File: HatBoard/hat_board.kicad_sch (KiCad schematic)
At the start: 18 parts, among them J10 Conn_02x02_Counter_Clockwise, J13 DF11 FC Connection, J14 Conn_02x02_Counter_Clockwise, J15 Conn_02x02_Counter_Clockwise, J19 DF11 FC Connection, J20 DF11 FC Connection, J21 DF11 FC Connection, J9 Conn_02x02_Counter_Clockwise, U10 VEML7700, U12 DRV2605LDGS, U27 TMP112AIDRLR

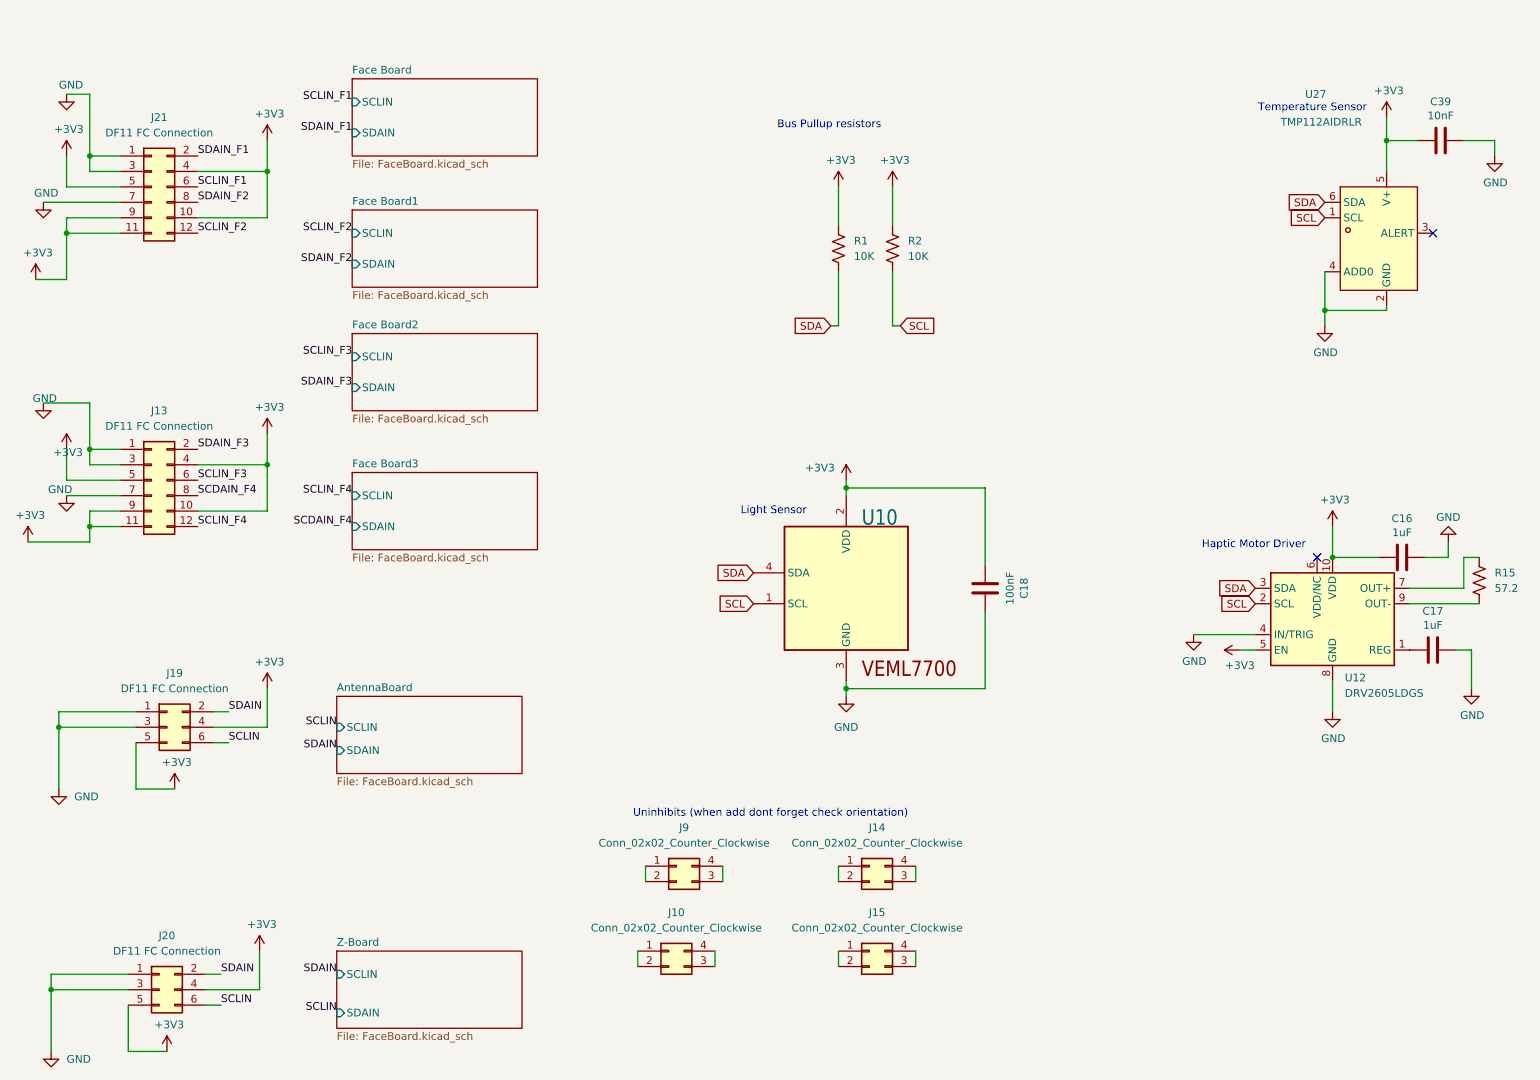
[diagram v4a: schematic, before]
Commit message: placement for face baord attachment
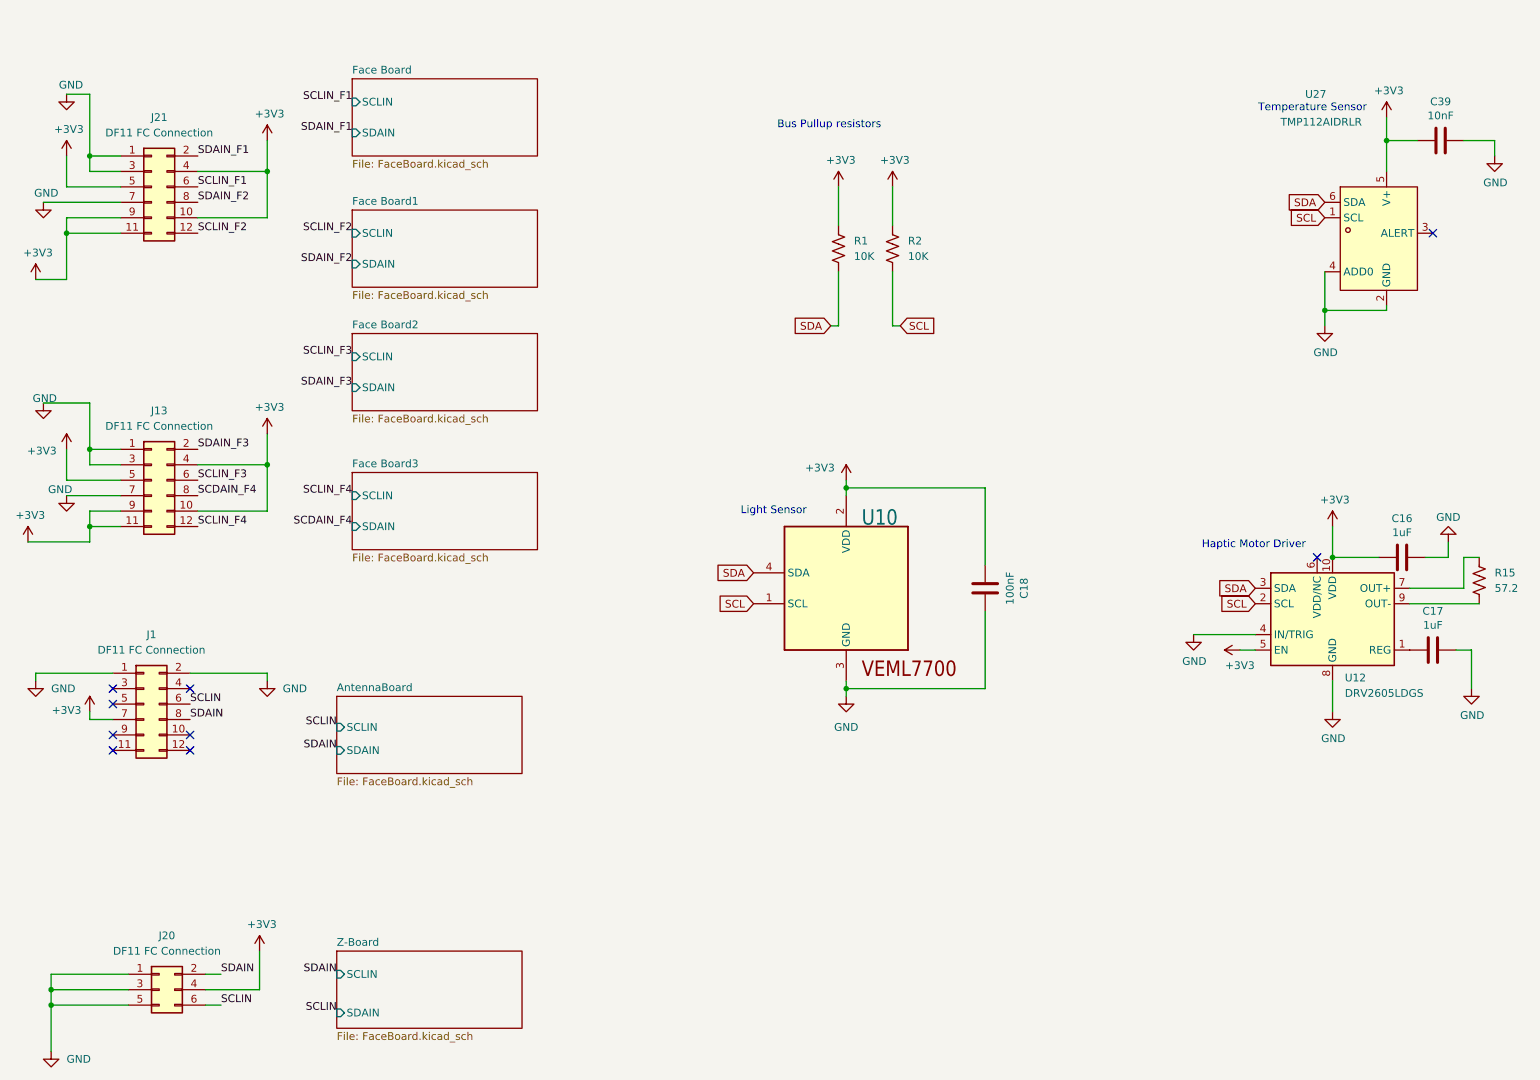
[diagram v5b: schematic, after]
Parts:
- removed J10, J14, J15, J9: Conn_02x02_Counter_Clockwise, symbol Connector_Generic:Conn_02x02_Counter_Clockwise
- removed J19: DF11 FC Connection, symbol Connector_Generic:Conn_02x03_Odd_Even
- added J1: DF11 FC Connection, easyeda2kicad:CONN-TH_DF11-12DS-2DSA-05, symbol Connector_Generic:Conn_02x06_Odd_Even
- J13, J20, J21: footprint (none) -> easyeda2kicad:CONN-TH_DF11-12DS-2DSA-05
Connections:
- net +3V3: now also J1.7 (Pin_7); no longer J20.5 (Pin_5)
- net GND: now also J20.5 (Pin_5), J1.1 (Pin_1), J1.2 (Pin_2)
- net SCLIN: now also J1.6 (Pin_6)
- net SDAIN: now also J1.8 (Pin_8)
- no-connect marks 2 -> 9
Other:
- note removed: "Uninhibits (when add dont forget check orientation)"

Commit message: updated schematic
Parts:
- added D1, D2, D3, D4: 1N4148WT, Diode_SMD:D_SOD-523, symbol Diode:1N4148WT
- added J2: Conn_01x04, Connector_PinHeader_2.00mm:PinHeader_1x04_P2.00mm_Vertical, symbol Connector_Generic:Conn_01x04
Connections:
- net +3V3: now also D1.2 (A), D2.2 (A), D3.2 (A), D4.2 (A); no longer J1.7 (Pin_7), J13.10 (Pin_10), J13.11 (Pin_11), J13.4 (Pin_4), J13.5 (Pin_5), J13.9 (Pin_9), J20.4 (Pin_4), J21.10 (Pin_10), J21.11 (Pin_11), J21.4 (Pin_4), J21.5 (Pin_5), J21.9 (Pin_9)
- net GND: now also J2.1 (Pin_1), J2.4 (Pin_4); no longer J13.3 (Pin_3), J20.1 (Pin_1), J20.3 (Pin_3), J21.3 (Pin_3)
- net SCL: now also J2.2 (Pin_2)
- net SDA: now also J2.3 (Pin_3)
- net SCLIN renamed SCLINZ
- net SCLINZ: no longer J1.6 (Pin_6)
- net SDAIN renamed SDAINZ
- net SDAINZ: no longer J1.8 (Pin_8)
- new net: D3.1 (K), J1.7 (Pin_7)
- new net: D2.1 (K), J13.10 (Pin_10), J13.4 (Pin_4)
- new net: D4.1 (K), J20.4 (Pin_4)
- new net: D1.1 (K), J21.10 (Pin_10), J21.4 (Pin_4)
- new net SCLIN_ANT: J1.6 (Pin_6)
- new net SDAIN_ANT: J1.8 (Pin_8)
- no-connect marks 9 -> 19
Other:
- moved on the sheet: J20

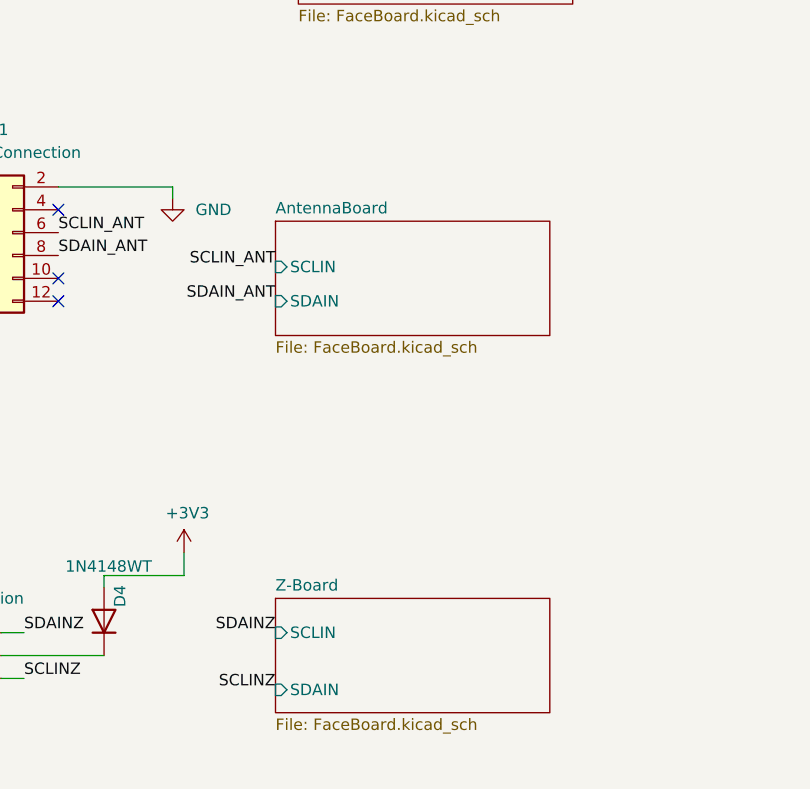
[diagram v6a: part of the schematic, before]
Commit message: corrected PCB design
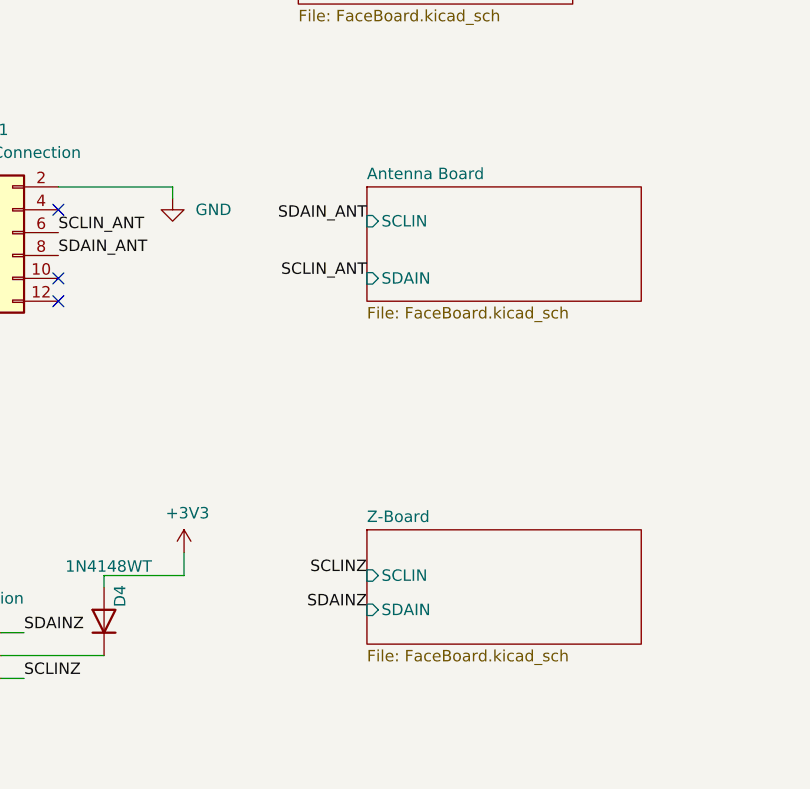
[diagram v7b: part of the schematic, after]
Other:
- removed sheet AntennaBoard
- added sheet Antenna Board (FaceBoard.kicad_sch)
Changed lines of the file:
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@@
 		)
 	)
-	(label "SDAINZ"
-		(at 64.77 172.72 180)
+	(label "SDAIN_ANT"
+		(at 74.93 127 180)
 		(effects
 			(font
@@
 		)
 	)
-	(label "SCLIN_ANT"
-		(at 64.77 132.08 180)
+	(label "SCLINZ"
+		(at 74.93 166.37 180)
 		(effects
 			(font
@@
 		)
 	)
-	(label "SDAIN_ANT"
-		(at 64.77 135.89 180)
+	(label "SDAINZ"
+		(at 74.93 170.18 180)
 		(effects
 			(font
@@
 		)
 	)
-	(label "SCLINZ"
-		(at 64.77 179.07 180)
+	(label "SCLIN_ANT"
+		(at 74.93 133.35 180)
 		(effects
 			(font
@@
 	)
 	(sheet
-		(at 64.77 168.91)
+		(at 74.93 123.19)
 		(size 30.48 12.7)
 		(exclude_from_sim no)
@@
 			(color 0 0 0 0.0000)
 		)
-		(property "Sheetname" "Z-Board"
-			(at 64.77 168.1984 0)
+		(property "Sheetname" "Antenna Board"
+			(at 74.93 122.4784 0)
 			(effects
 				(font
@@
 		)
 		(property "Sheetfile" "FaceBoard.kicad_sch"
-			(at 64.77 182.1946 0)
+			(at 74.93 136.4746 0)
 			(effects
 				(font
@@
 		)
 		(pin "SCLIN" input
-			(at 64.77 172.72 180)
+			(at 74.93 127 180)
 			(effects
 				(font
@@
 		)
 		(pin "SDAIN" input
-			(at 64.77 179.07 180)
+			(at 74.93 133.35 180)
 			(effects
 				(font
@@
 	)
 	(sheet
-		(at 64.77 127)
+		(at 74.93 161.29)
 		(size 30.48 12.7)
 		(exclude_from_sim no)
@@
 			(color 0 0 0 0.0000)
 		)
-		(property "Sheetname" "AntennaBoard"
-			(at 64.77 126.2884 0)
+		(property "Sheetname" "Z-Board"
+			(at 74.93 160.5784 0)
 			(effects
 				(font
@@
 		)
 		(property "Sheetfile" "FaceBoard.kicad_sch"
-			(at 64.77 140.2846 0)
+			(at 74.93 174.5746 0)
 			(effects
 				(font
@@
 		)
 		(pin "SCLIN" input
-			(at 64.77 132.08 180)
+			(at 74.93 166.37 180)
 			(effects
 				(font
@@
 		)
 		(pin "SDAIN" input
-			(at 64.77 135.89 180)
+			(at 74.93 170.18 180)
 			(effects
 				(font

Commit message: from mirror board in schem to bwllo bowrd
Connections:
- net GND: now also J1.11 (Pin_11), J1.12 (Pin_12), J13.11 (Pin_11), J13.5 (Pin_5), J21.11 (Pin_11), J21.5 (Pin_5); no longer J1.1 (Pin_1), J1.2 (Pin_2), J13.1 (Pin_1), J13.7 (Pin_7), J21.1 (Pin_1), J21.7 (Pin_7)
- net SCDAIN_F4: now also J13.12 (Pin_12); no longer J13.8 (Pin_8)
- net SCLIN_ANT: now also J1.7 (Pin_7); no longer J1.6 (Pin_6)
- net SCLIN_F2: now also J21.8 (Pin_8); no longer J21.12 (Pin_12)
- net SCLIN_F4: now also J13.8 (Pin_8); no longer J13.12 (Pin_12)
- net SDAIN_ANT: now also J1.5 (Pin_5); no longer J1.8 (Pin_8)
- net SDAIN_F2: now also J21.12 (Pin_12); no longer J21.8 (Pin_8)
- net at D3.1 (K): now also J1.6 (Pin_6); no longer J1.7 (Pin_7)
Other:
- moved on the sheet: D3
